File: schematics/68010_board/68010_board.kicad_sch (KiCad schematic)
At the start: 7 parts, among them IC1 MC68010R, J1 48-bit bus, SW1 CLK DIP Switch, SW2 Reset, U1 SN74HC4040N, U2 DS1813-5, X1 Crystal Oscillator

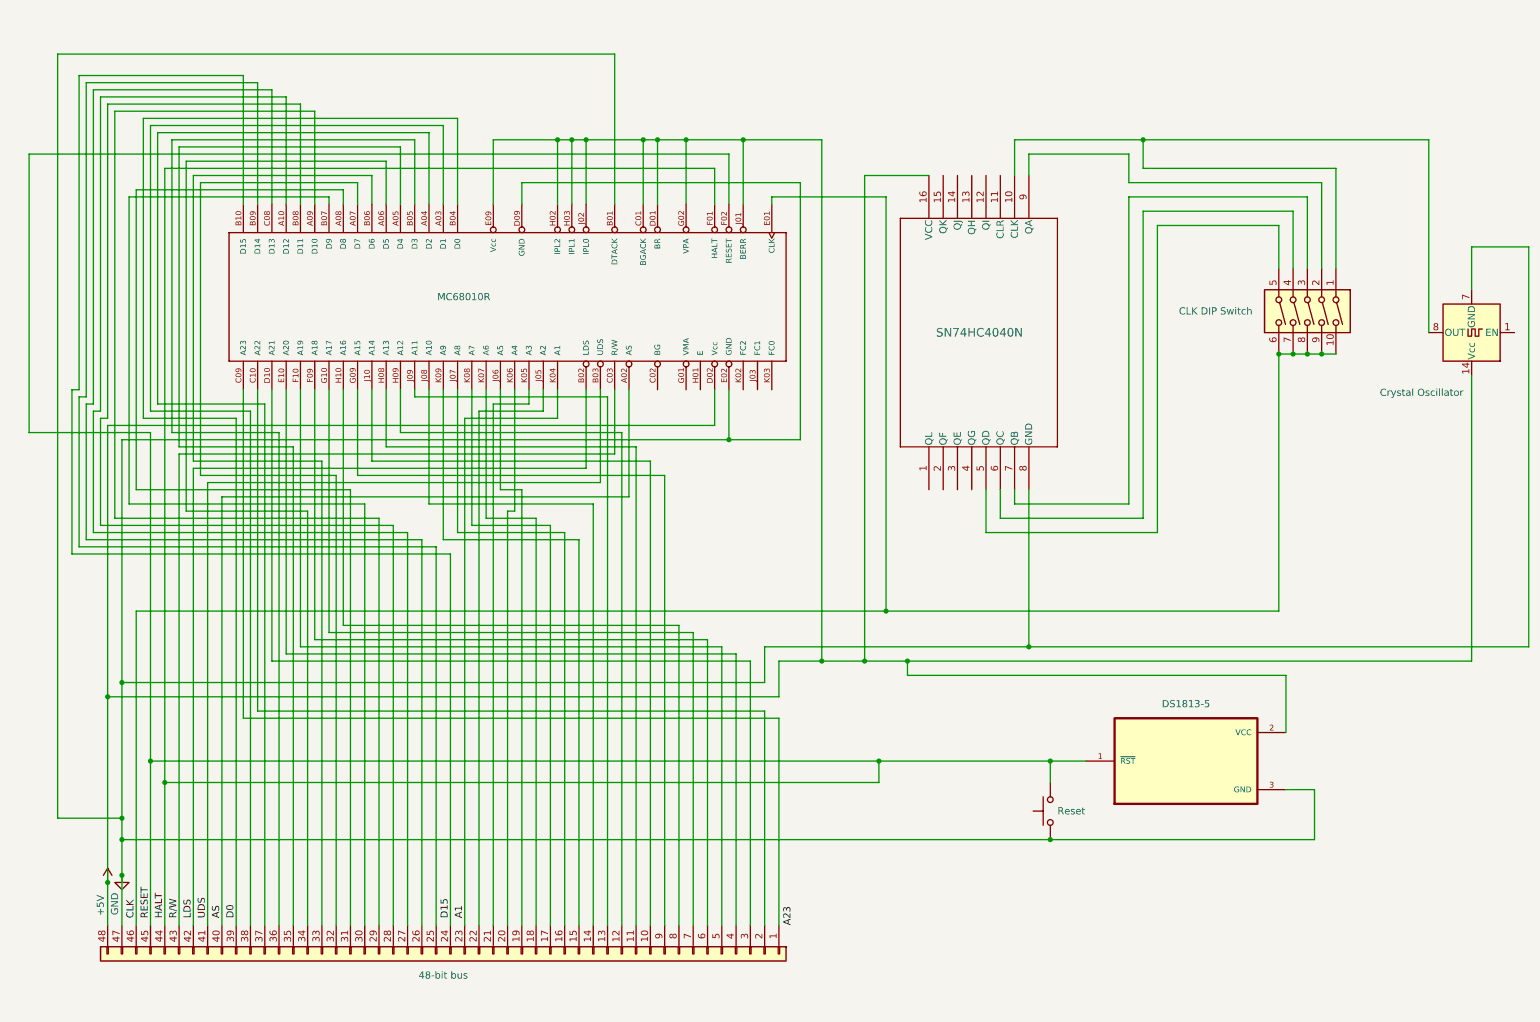
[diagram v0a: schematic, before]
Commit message: aether: Add updated schematics (64->80 pin header, future-proofing)
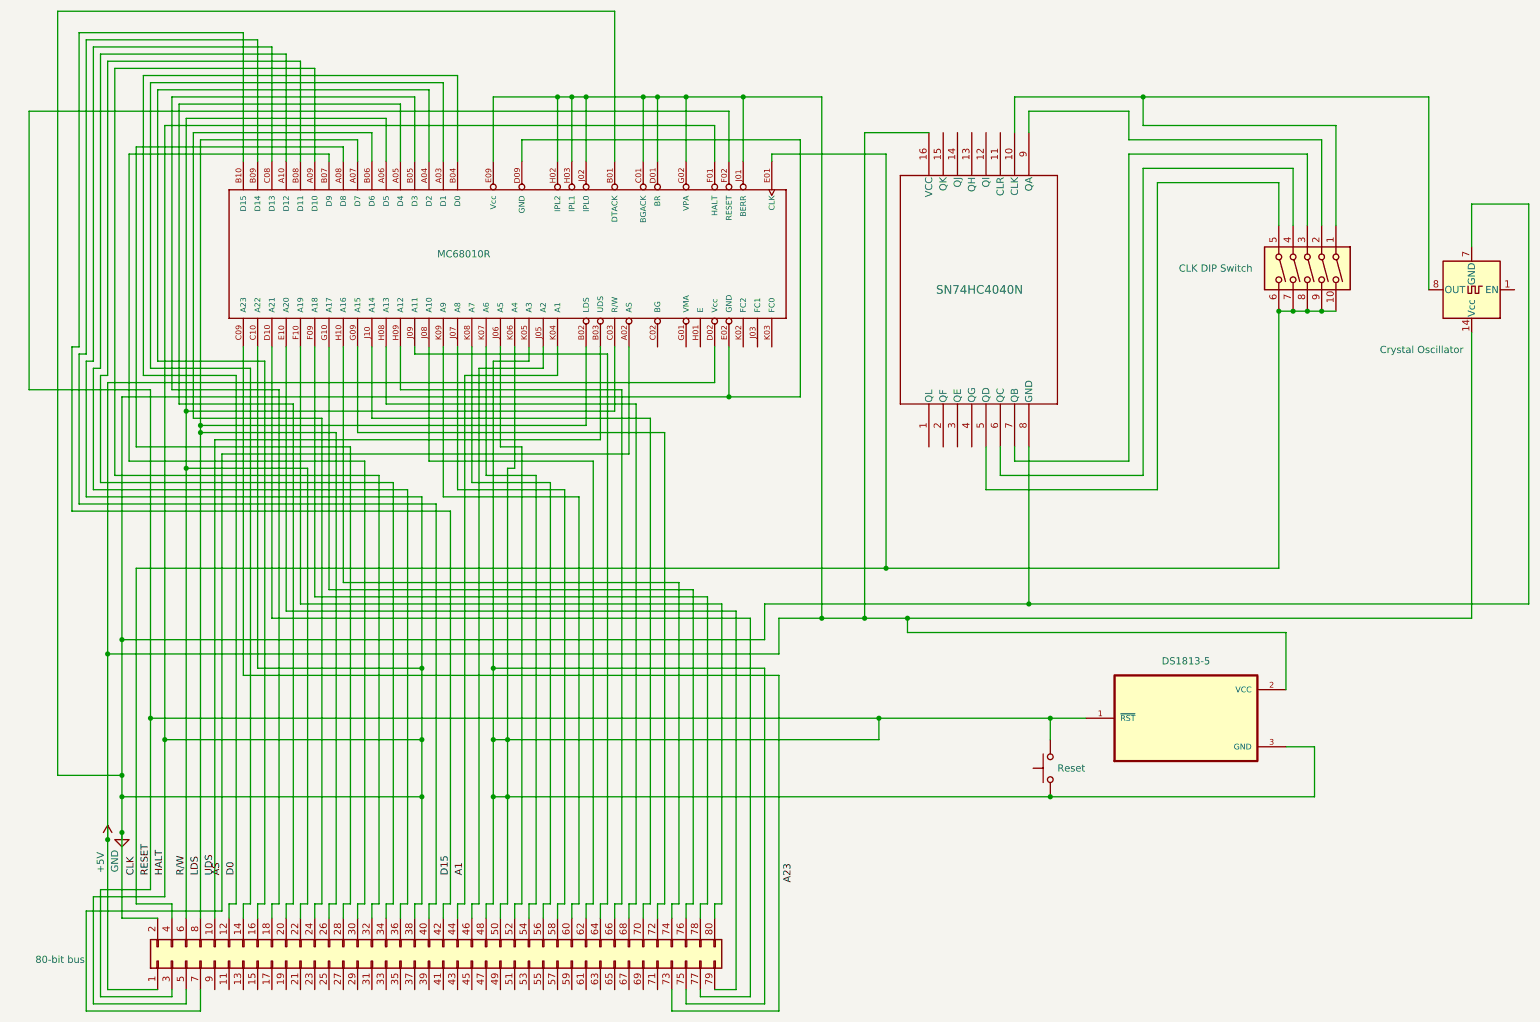
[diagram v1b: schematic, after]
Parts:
- removed J1: 48-bit bus, parts:PinHeader_1x48_P2.54mm_Horizontal, symbol Connector_Generic:Conn_01x48
- added J2: 80-bit bus, Connector_PinHeader_2.00mm:PinHeader_2x40_P2.00mm_Horizontal, symbol Connector_Generic:Conn_02x40_Odd_Even
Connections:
- net +5V: now also J2.1 (Pin_1)
- net A1: now also J2.44 (Pin_44)
- net AS: now also J2.7 (Pin_7)
- net CLK: now also J2.4 (Pin_4)
- net D0: now also J2.12 (Pin_12)
- net D15: now also J2.42 (Pin_42)
- net GND: now also IC1.C08 (D13), IC1.C10 (A22), IC1.F01 (HALT), J2.2 (Pin_2), J2.38 (Pin_38), J2.5 (Pin_5); no longer SW2.1, U2.3 (GND)
- net LDS: now also IC1.A07 (D7), J2.26 (Pin_26), J2.8 (Pin_8)
- net R/W: now also IC1.A06 (D5), J2.22 (Pin_22), J2.6 (Pin_6)
- net UDS: now also J2.10 (Pin_10)
- net at IC1.C09 (A23): now also J2.73 (Pin_73)
- net at IC1.J10 (A14): now also J2.70 (Pin_70)
- net at IC1.H08 (A13): now also J2.68 (Pin_68)
- net at IC1.H09 (A12): now also J2.66 (Pin_66)
- net at IC1.J09 (A11): now also J2.64 (Pin_64)
- net at IC1.J08 (A10): now also J2.62 (Pin_62)
- net at IC1.K09 (A9): now also J2.60 (Pin_60)
- net at IC1.J07 (A8): now also J2.58 (Pin_58)
- net at IC1.K08 (A7): now also J2.56 (Pin_56)
- net at IC1.K07 (A6): now also J2.54 (Pin_54)
- net at IC1.J06 (A5): now also J2.52 (Pin_52)
- net RESET: now reaches IC1.K06 (A4)
- net RESET: now also IC1.F02 (RESET), IC1.K05 (A3), SW2.1, SW2.2, U2.1 (~{RST}), U2.3 (GND), J2.3 (Pin_3), J2.48 (Pin_48), J2.50 (Pin_50), J2.75 (Pin_75)
- net at IC1.J05 (A2): now also J2.46 (Pin_46)
- net at IC1.B09 (D14): now also J2.40 (Pin_40)
- net at IC1.A10 (D12): now also J2.36 (Pin_36)
- net at IC1.B08 (D11): now also J2.34 (Pin_34)
- net at IC1.A09 (D10): now also J2.32 (Pin_32)
- net at IC1.D10 (A21): now also J2.77 (Pin_77)
- net at IC1.B07 (D9): now also J2.30 (Pin_30)
- net at IC1.A08 (D8): now also J2.28 (Pin_28)
- net at IC1.B06 (D6): now also J2.24 (Pin_24)
- net at IC1.A05 (D4): now also J2.20 (Pin_20)
- net at IC1.B05 (D3): now also J2.18 (Pin_18)
- net at IC1.A04 (D2): now also J2.16 (Pin_16)
- net at IC1.A03 (D1): now also J2.14 (Pin_14)
- net at IC1.E10 (A20): now also J2.79 (Pin_79)
- net at IC1.F10 (A19): now also J2.80 (Pin_80)
- net at IC1.F09 (A18): now also J2.78 (Pin_78)
- net at IC1.G10 (A17): now also J2.76 (Pin_76)
- net at IC1.H10 (A16): now also J2.74 (Pin_74)
- net at IC1.G09 (A15): now also J2.72 (Pin_72)
- removed net HALT: IC1.F01 (HALT), IC1.F02 (RESET), SW2.2, U2.1 (~{RST})
